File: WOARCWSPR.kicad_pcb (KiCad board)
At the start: 2 copper layers, 65 x 30.5 mm, 27 parts, among them J1 TP2, J2 Raspberry_Pi_2_3, J3 TP2, J4 Conn_Coaxial, J5 LPF_OUT, J6 LPF_IN, J7 TP1, J8 TP2, Q1 BS170, SW1 SW_Push_Dual

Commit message: Correct pin layout for filter board
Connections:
- C3 pad 2: Net-(J6-Pin_3) -> Net-(J6-Pin_1)
- J6 pad 1: GND -> Net-(J6-Pin_1)
- J6 pad 2: GND -> Net-(J6-Pin_1)
- J6 pad 3: Net-(J6-Pin_3) -> GND
- J6 pad 4: Net-(J6-Pin_3) -> GND
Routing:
- net Net-(J6-Pin_3): track 18.0 -> 0.00 mm
- net GND: track 82.5 -> 100.5 mm
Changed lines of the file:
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@@
 	(net 36 "Net-(Q1-G)")
 	(net 37 "Net-(J7-Pin_1)")
-	(net 38 "Net-(J6-Pin_3)")
+	(net 38 "Net-(J6-Pin_1)")
 	(net 39 "Net-(J8-Pin_1)")
 	(net 40 "Net-(R3-Pad1)")
@@
 			)
 		)
-		(property "Description" "Unpolarized capacitor"
+		(property "Description" "Polarized capacitor"
 			(at 0 0 0)
 			(unlocked yes)
@@
 			)
 		)
-		(property ki_fp_filters "C_*")
+		(property ki_fp_filters "CP_*")
 		(sheetname "Root")
 		(sheetfile "WOARCWSPR.kicad_sch")
@@
 			(layers "*.Cu" "*.Mask")
 			(remove_unused_layers no)
-			(net 38 "Net-(J6-Pin_3)")
+			(net 38 "Net-(J6-Pin_1)")
 			(pintype "passive")
 		)
@@
 			(layers "*.Cu" "*.Mask")
 			(remove_unused_layers no)
-			(net 1 "GND")
+			(net 38 "Net-(J6-Pin_1)")
 			(pinfunction "Pin_1")
 			(pintype "passive")
@@
 			(layers "*.Cu" "*.Mask")
 			(remove_unused_layers no)
-			(net 1 "GND")
+			(net 38 "Net-(J6-Pin_1)")
 			(pinfunction "Pin_2")
 			(pintype "passive")
@@
 			(layers "*.Cu" "*.Mask")
 			(remove_unused_layers no)
-			(net 38 "Net-(J6-Pin_3)")
+			(net 1 "GND")
 			(pinfunction "Pin_3")
 			(pintype "passive")
@@
 			(layers "*.Cu" "*.Mask")
 			(remove_unused_layers no)
-			(net 38 "Net-(J6-Pin_3)")
+			(net 1 "GND")
 			(pinfunction "Pin_4")
 			(pintype "passive")
@@
 	)
 	(segment
+		(start 221.9 56.8)
+		(end 220.8 57.9)
+		(width 0.2)
+		(layer "F.Cu")
+		(net 1)
+	)
+	(segment
 		(start 161.6 37.2)
 		(end 161.5 37.3)
@@
 	)
 	(segment
+		(start 220.8 57.9)
+		(end 214.5 57.9)
+		(width 0.2)
+		(layer "F.Cu")
+		(net 1)
+	)
+	(segment
+		(start 209.32 52.72)
+		(end 209 52.72)
+		(width 0.2)
+		(layer "F.Cu")
+		(net 1)
+	)
+	(segment
 		(start 178.035 34.775)
 		(end 178.035 34.365)
@@
 	)
 	(segment
+		(start 214.5 57.9)
+		(end 209.32 52.72)
+		(width 0.2)
+		(layer "F.Cu")
+		(net 1)
+	)
+	(segment
 		(start 204.585 31.085)
 		(end 207.365 31.085)
@@
 	)
 	(segment
+		(start 209 52.72)
+		(end 209 50.18)
+		(width 0.2)
+		(layer "F.Cu")
+		(net 1)
+	)
+	(segment
 		(start 178.035 34.365)
 		(end 178.8 33.6)
@@
 	)
 	(segment
-		(start 221.9 56.8)
-		(end 220.8 57.9)
-		(width 0.2)
-		(layer "F.Cu")
-		(net 38)
-	)
-	(segment
-		(start 220.8 57.9)
-		(end 214.5 57.9)
-		(width 0.2)
-		(layer "F.Cu")
-		(net 38)
-	)
-	(segment
-		(start 209.32 52.72)
-		(end 209 52.72)
-		(width 0.2)
-		(layer "F.Cu")
-		(net 38)
-	)
-	(segment
-		(start 214.5 57.9)
-		(end 209.32 52.72)
-		(width 0.2)
-		(layer "F.Cu")
-		(net 38)
-	)
-	(segment
-		(start 209 52.72)
-		(end 209 50.18)
-		(width 0.2)
-		(layer "F.Cu")
-		(net 38)
-	)
-	(segment
 		(start 220 53.8)
 		(end 220 53.4)
@@
 		(min_thickness 0.25)
 		(filled_areas_thickness no)
-		(fill yes
+		(fill
 			(thermal_gap 0.5)
 			(thermal_bridge_width 0.5)

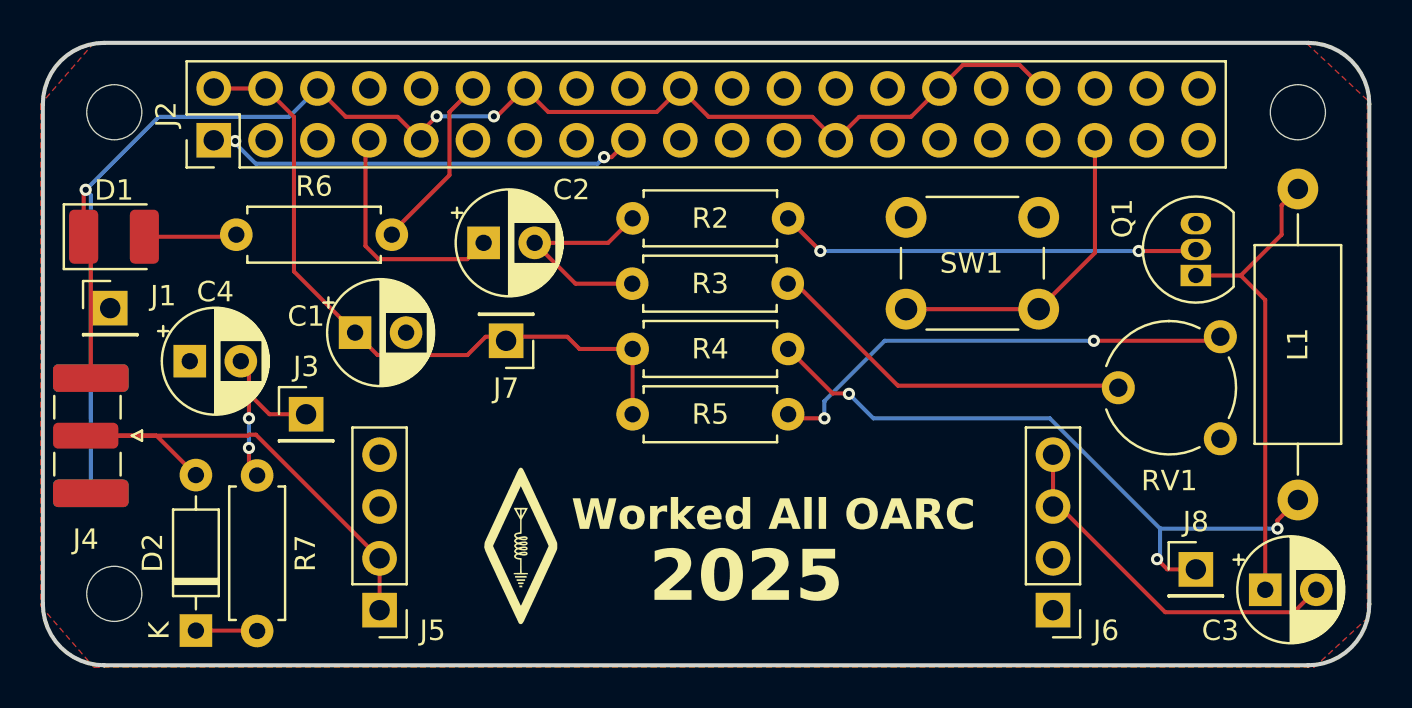
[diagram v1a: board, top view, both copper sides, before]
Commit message: Change to ceramic cap footprints
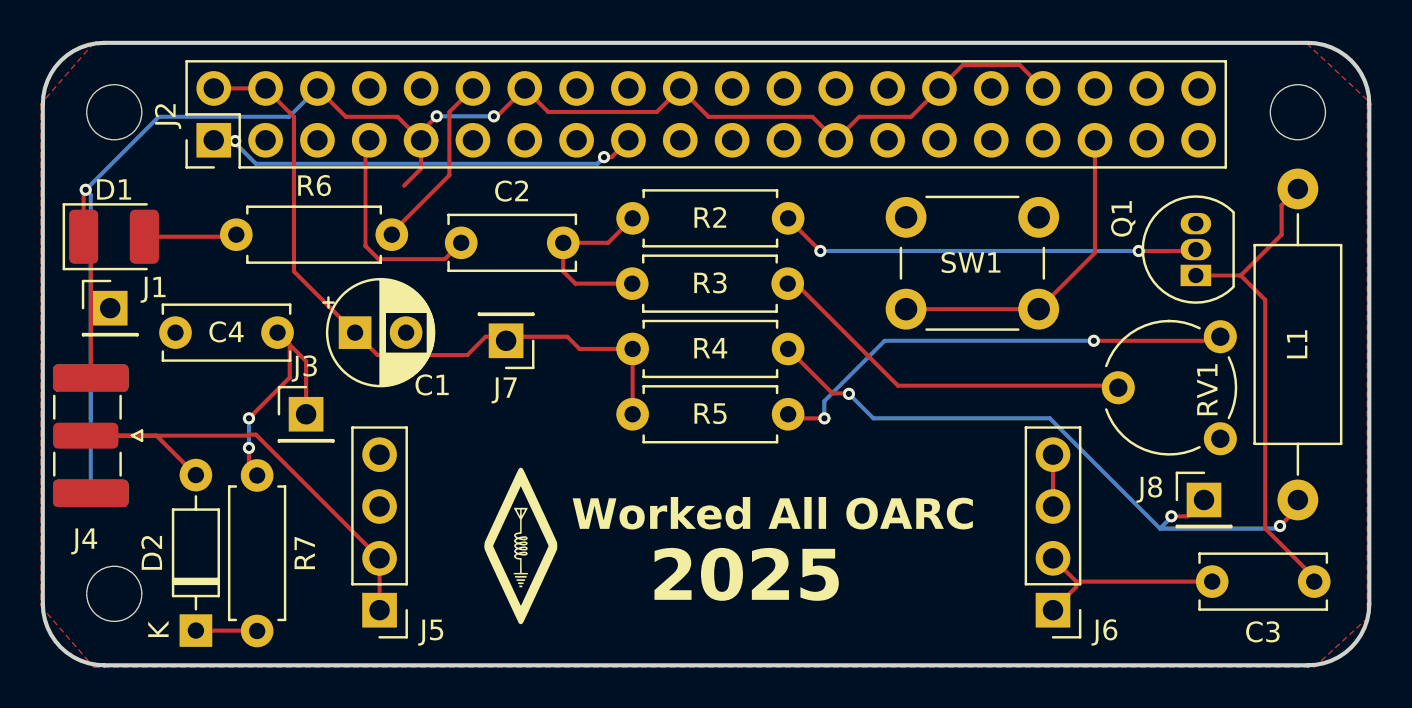
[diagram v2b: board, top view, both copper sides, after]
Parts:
- C2, C3, C4: footprint Capacitor_THT:CP_Radial_D5.0mm_P2.50mm -> Capacitor_THT:C_Disc_D6.0mm_W2.5mm_P5.00mm
- moved J8 3.42 mm to (216.4, 52.4)
- moved C3 2.43 mm to (221.8, 56.4), turned to 180 degrees
- moved C4 1.57 mm to (166.0, 44.2)
- moved C2 1.10 mm to (180.0, 39.8)
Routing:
- net GND: track 100.5 -> 87.9 mm
- net Net-(J6-Pin_1): track 0.00 -> 10.1 mm
- net Net-(J3-Pin_1): track 9.15 -> 12.8 mm
- net Net-(C2-Pad2): track 10.9 -> 8.93 mm
- net Net-(J2-GCLK0/GPIO4): track 11.7 -> 10.6 mm
- net Net-(J8-Pin_1): track 33.1 -> 32.2 mm
- net Net-(Q1-D): track 23.5 -> 24.1 mm

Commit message: Update version number to 1.1
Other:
- board text added: "WSPRHATZERO Version 1.1"
- board text removed: "WSPRHATZERO Version 1.0"
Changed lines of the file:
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@@
 		)
 	)
-	(gr_text "WSPRHATZERO\nVersion 1.0"
+	(gr_text "WSPRHATZERO\nVersion 1.1"
 		(at 207 55.6 0)
 		(layer "B.SilkS")
@@
 			(justify left bottom mirror)
 		)
-		(render_cache "WSPRHATZERO\nVersion 1.0" 0
+		(render_cache "WSPRHATZERO\nVersion 1.1" 0
 			(polygon
 				(pts
@@
 			(polygon
 				(pts
-					(xy 198.655605 54.182369) (xy 198.720692 54.199027) (xy 198.780439 54.226365) (xy 198.834093 54.264035)
-					(xy 198.880899 54.311689) (xy 198.894849 54.329733) (xy 198.92973 54.388186) (xy 198.952989 54.447009)
-					(xy 198.97109 54.515553) (xy 198.981933 54.577721) (xy 198.989605 54.646684) (xy 198.994166 54.722694)
-					(xy 198.995579 54.78448) (xy 198.995673 54.806006) (xy 198.994415 54.882598) (xy 198.990613 54.953276)
-					(xy 198.98422 55.018114) (xy 198.975193 55.077189) (xy 198.960137 55.143044) (xy 198.940808 55.200158)
-					(xy 198.911849 55.257367) (xy 198.875496 55.306972) (xy 198.832999 55.348743) (xy 198.784867 55.382444)
-					(xy 198.731609 55.407843) (xy 198.673736 55.424703) (xy 198.611758 55.43279) (xy 198.585931 55.433515)
-					(xy 198.526976 55.429733) (xy 198.461086 55.415316) (xy 198.400797 55.390295) (xy 198.346437 55.354857)
-					(xy 198.298328 55.309187) (xy 198.27672 55.282573) (xy 198.242383 55.224012) (xy 198.21923 55.16515)
-					(xy 198.201029 55.0969) (xy 198.190023 55.035386) (xy 198.18217 54.967601) (xy 198.177464 54.893427)
-					(xy 198.175994 54.833534) (xy 198.175896 54.812748) (xy 198.175956 54.807765) (xy 198.410956 54.807765)
-					(xy 198.411814 54.870403) (xy 198.414306 54.930715) (xy 198.419272 54.997468) (xy 198.427511 55.063641)
-					(xy 198.441437 55.122545) (xy 198.469425 55.174469) (xy 198.517621 55.216103) (xy 198.579661 55.232047)
-					(xy 198.585931 55.232161) (xy 198.644486 55.220899) (xy 198.695202 55.183719) (xy 198.723684 55.139545)
-					(xy 198.741025 55.080096) (xy 198.750942 55.012929) (xy 198.756771 54.942808) (xy 198.75964 54.876693)
-					(xy 198.760614 54.804541) (xy 198.759774 54.738998) (xy 198.757331 54.676283) (xy 198.752444 54.60729)
-					(xy 198.745609 54.548066) (xy 198.733807 54.489664) (xy 198.730425 54.479503) (xy 198.703026 54.426191)
-					(xy 198.659525 54.386118) (xy 198.598338 54.367134) (xy 198.585931 54.366662) (xy 198.527947 54.378408)
-					(xy 198.48041 54.412837) (xy 198.447885 54.462796) (xy 198.430544 54.523139) (xy 198.421843 54.581354)
-					(xy 198.415592 54.651944) (xy 198.412354 54.718975) (xy 198.410995 54.792401) (xy 198.410956 54.807765)
-					(xy 198.175956 54.807765) (xy 198.17661 54.753096) (xy 198.179798 54.679206) (xy 198.185574 54.611609)
-					(xy 198.193972 54.550135) (xy 198.208211 54.48164) (xy 198.226667 54.422108) (xy 198.254477 54.362027)
-					(xy 198.25972 54.35318) (xy 198.296074 54.303556) (xy 198.338579 54.261737) (xy 198.386733 54.22797)
-					(xy 198.440032 54.202504) (xy 198.497973 54.185588) (xy 198.560053 54.177468) (xy 198.585931 54.176739)
-				)
-			)
+					(xy 198.644549 54.574464) (xy 198.644549 55.396) (xy 198.40949 55.396) (xy 198.40949 54.204876)
+					(xy 198.565708 54.204876) (xy 198.589276 54.266019) (xy 198.625313 54.316963) (xy 198.673752 54.35764)
+					(xy 198.734527 54.387984) (xy 198.791984 54.404773) (xy 198.857257 54.414873) (xy 198.930314 54.418247)
+					(xy 198.930314 54.574464)
+				)
+			)

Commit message: Swap to 3mm THT LED
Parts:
- D1: footprint LED_SMD:LED_1210_3225Metric_Pad1.42x2.65mm_HandSolder -> LED_THT:LED_D3.0mm
- moved D1 1.55 mm to (161.6, 38.8)
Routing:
- net GND: track 87.9 -> 88.5 mm
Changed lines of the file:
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@@
 		)
 	)
-	(footprint "LED_SMD:LED_1210_3225Metric_Pad1.42x2.65mm_HandSolder"
+	(footprint "LED_THT:LED_D3.0mm"
 		(layer "F.Cu")
-		(at 162.9875 39.5)
-		(descr "LED SMD 1210 (3225 Metric), square (rectangular) end terminal, IPC_7351 nominal, (Body size source: http://www.tortai-tech.com/upload/download/2011102023233369053.pdf), generated with kicad-footprint-generator")
-		(tags "LED handsolder")
+		(at 161.6 38.8)
+		(descr "LED, diameter 3.0mm, 2 pins, generated by kicad-footprint-generator")
+		(tags "LED")
 		(property "Reference" "D1"
-			(at 0 -2.28 0)
+			(at 1.27 -2.96 0)
 			(layer "F.SilkS")
 			(effects
@@
 		)
 		(property "Value" "LED"
-			(at 0 2.28 0)
+			(at 1.27 2.96 0)
 			(layer "F.Fab")
 			(effects
@@
 			)
 		)
-		(property "Footprint" "LED_SMD:LED_1210_3225Metric_Pad1.42x2.65mm_HandSolder"
+		(property "Footprint" "LED_THT:LED_D3.0mm"
 			(at 0 0 0)
-			(unlocked yes)
 			(layer "F.Fab")
 			(hide yes)
@@
 		(property "Datasheet" ""
 			(at 0 0 0)
-			(unlocked yes)
 			(layer "F.Fab")
 			(hide yes)
@@
 		(property "Description" "Light emitting diode"
 			(at 0 0 0)
-			(unlocked yes)
 			(layer "F.Fab")
 			(hide yes)
@@
 		(sheetname "Root")
 		(sheetfile "WOARCWSPR.kicad_sch")
-		(attr smd)
+		(attr through_hole)
 		(fp_line
-			(start -2.46 -1.585)
-			(end -2.46 1.585)
+			(start -0.29 -1.236)
+			(end -0.29 -1.08)
 			(stroke
 				(width 0.12)
@@
 		)
 		(fp_line
-			(start -2.46 1.585)
-			(end 1.6 1.585)
+			(start -0.29 1.08)
+			(end -0.29 1.236)
 			(stroke
 				(width 0.12)
@@
 			(layer "F.SilkS")
 		)
-		(fp_line
-			(start 1.6 -1.585)
-			(end -2.46 -1.585)
+		(fp_arc
+			(start -0.29 -1.235516)
+			(mid 1.365624 -1.987701)
+			(end 2.941397 -1.080061)
 			(stroke
 				(width 0.12)
@@
 			(layer "F.SilkS")
 		)
-		(fp_line
-			(start -2.45 -1.58)
-			(end 2.45 -1.58)
+		(fp_arc
+			(start 0.229039 -1.08)
+			(mid 1.269965 -1.5)
+			(end 2.31091 -1.080049)
 			(stroke
-				(width 0.05)
+				(width 0.12)
 				(type solid)
 			)
-			(layer "F.CrtYd")
+			(layer "F.SilkS")
 		)
-		(fp_line
-			(start -2.45 1.58)
-			(end -2.45 -1.58)
+		(fp_arc
+			(start 2.31091 1.080049)
+			(mid 1.269965 1.5)
+			(end 0.229039 1.08)
 			(stroke
-				(width 0.05)
+				(width 0.12)
 				(type solid)
 			)
-			(layer "F.CrtYd")
+			(layer "F.SilkS")
+		)
+		(fp_arc
+			(start 2.941397 1.080061)
+			(mid 1.365624 1.987701)
+			(end -0.29 1.235516)
+			(stroke
+				(width 0.12)
+				(type solid)
+			)
+			(layer "F.SilkS")
 		)
 		(fp_line
-			(start 2.45 -1.58)
-			(end 2.45 1.58)
+			(start -1.15 -2.21)
+			(end -1.15 2.21)
 			(stroke
 				(width 0.05)
@@
 		)
 		(fp_line
-			(start 2.45 1.58)
-			(end -2.45 1.58)
+			(start -1.15 2.21)
+			(end 3.69 2.21)
 			(stroke
 				(width 0.05)
@@
 		)
 		(fp_line
-			(start -1.6 -0.625)
-			(end -1.6 1.25)
+			(start 3.69 -2.21)
+			(end -1.15 -2.21)
 			(stroke
-				(width 0.1)
+				(width 0.05)
 				(type solid)
 			)
-			(layer "F.Fab")
+			(layer "F.CrtYd")
 		)
 		(fp_line
-			(start -1.6 1.25)
-			(end 1.6 1.25)
+			(start 3.69 2.21)
+			(end 3.69 -2.21)
 			(stroke
-				(width 0.1)
+				(width 0.05)
 				(type solid)
 			)
-			(layer "F.Fab")
+			(layer "F.CrtYd")
 		)
 		(fp_line
-			(start -0.975 -1.25)
-			(end -1.6 -0.625)
+			(start -0.23 -1.16619)
+			(end -0.23 1.16619)
 			(stroke
 				(width 0.1)
@@
 			(layer "F.Fab")
 		)
-		(fp_line
-			(start 1.6 -1.25)
-			(end -0.975 -1.25)
+		(fp_arc
+			(start -0.23 -1.16619)
+			(mid 3.17 -0.000037)
+			(end -0.229955 1.166249)
 			(stroke
 				(width 0.1)
@@
 			(layer "F.Fab")
 		)
-		(fp_line
-			(start 1.6 1.25)
-			(end 1.6 -1.25)
+		(fp_circle
+			(center 1.27 0)
+			(end 2.77 0)
 			(stroke
 				(width 0.1)
 				(type solid)
 			)
+			(fill none)
 			(layer "F.Fab")
 		)
 		(fp_text user "${REFERENCE}"
-			(at 0.0125 0.1 0)
+			(at 1.27 0 0)
 			(layer "F.Fab")
 			(effects
@@
 			)
 		)
-		(pad "1" smd roundrect
-			(at -1.4875 0)
-			(size 1.425 2.65)
-			(layers "F.Cu" "F.Paste" "F.Mask")
-			(roundrect_rratio 0.175439)
+		(pad "1" thru_hole rect
+			(at 0 0)
+			(size 1.8 1.8)
+			(drill 0.9)
+			(layers "*.Cu" "*.Mask")
+			(remove_unused_layers no)
 			(net 1 "GND")
 			(pinfunction "K")
 			(pintype "passive")
 		)
-		(pad "2" smd roundrect
-			(at 1.4875 0)
-			(size 1.425 2.65)
-			(layers "F.Cu" "F.Paste" "F.Mask")
-			(roundrect_rratio 0.175439)
+		(pad "2" thru_hole circle
+			(at 2.54 0)
+			(size 1.8 1.8)
+			(drill 0.9)
+			(layers "*.Cu" "*.Mask")
+			(remove_unused_layers no)
 			(net 5 "Net-(D1-A)")
 			(pinfunction "A")
 			(pintype "passive")
 		)
-		(model "${KICAD8_3DMODEL_DIR}/LED_SMD.3dshapes/LED_1210_3225Metric.wrl"
+		(model "${KICAD8_3DMODEL_DIR}/LED_THT.3dshapes/LED_D3.0mm.wrl"
 			(offset
 				(xyz 0 0 0)
@@
 	)
 	(segment
-		(start 161.85 40.05)
-		(end 161.85 46.425)
+		(start 162.202082 36.602082)
+		(end 161.5 37.304164)
 		(width 0.2)
 		(layer "F.Cu")
@@
 	)
 	(segment
-		(start 161.6 37.2)
-		(end 161.5 37.3)
+		(start 203.435 32.235)
+		(end 204.585 31.085)
 		(width 0.2)
 		(layer "F.Cu")
@@
 	)
 	(segment
-		(start 203.435 32.235)
-		(end 204.585 31.085)
+		(start 178.035 34.775)
+		(end 176.885 33.625)
 		(width 0.2)
 		(layer "F.Cu")
@@
 	)
 	(segment
-		(start 178.035 34.775)
-		(end 176.885 33.625)
+		(start 161.5 39.7)
+		(end 161.85 40.05)
 		(width 0.2)
 		(layer "F.Cu")
@@
 	)
 	(segment
-		(start 161.5 37.3)
-		(end 161.5 39.5)
-		(width 0.2)
-		(layer "F.Cu")
-		(net 1)
-	)
-	(segment
 		(start 178.035 36.165)
 		(end 177.2 37)
@@
 	)
 	(segment
-		(start 203.435 32.235)
-		(end 202.045 33.625)
+		(start 161.5 37.304164)
+		(end 161.5 39.7)
 		(width 0.2)
 		(layer "F.Cu")
@@
 	)
 	(segment
-		(start 181.75 33.6)
-		(end 183.115 32.235)
+		(start 203.435 32.235)
+		(end 202.045 33.625)
 		(width 0.2)
 		(layer "F.Cu")
@@
 	)
 	(segment
-		(start 161.5 39.5)
-		(end 161.5 39.7)
+		(start 181.75 33.6)
+		(end 183.115 32.235)
 		(width 0.2)
 		(layer "F.Cu")
@@
 	)
 	(segment
-		(start 161.5 39.7)
-		(end 161.85 40.05)
+		(start 181.6 33.6)
+		(end 181.75 33.6)
 		(width 0.2)
 		(layer "F.Cu")
@@
 	)
 	(segment
-		(start 181.6 33.6)
-		(end 181.75 33.6)
+		(start 161.85 40.05)
+		(end 161.85 46.425)
 		(width 0.2)
 		(layer "F.Cu")
@@
 	)
 	(via
-		(at 161.6 37.2)
+		(at 162.202082 36.602082)
 		(size 0.6)
 		(drill 0.3)
@@
 	)
 	(segment
-		(start 172.955 32.235)
-		(end 171.565 33.625)
+		(start 161.85 36.954164)
+		(end 161.85 48.4)
 		(width 0.2)
 		(layer "B.Cu")
@@
 	)
 	(segment
-		(start 161.85 37.45)
-		(end 161.6 37.2)
+		(start 171.565 33.625)
+		(end 172.955 32.235)
 		(width 0.2)
 		(layer "B.Cu")
@@
 	)
 	(segment
-		(start 178.8 33.6)
-		(end 181.6 33.6)
+		(start 162.202082 36.602082)
+		(end 161.85 36.954164)
 		(width 0.2)
 		(layer "B.Cu")
@@
 	)
 	(segment
-		(start 161.85 48.4)
-		(end 161.85 37.45)
+		(start 178.8 33.6)
+		(end 181.6 33.6)
 		(width 0.2)
 		(layer "B.Cu")
@@
 	)
 	(segment
-		(start 161.85 48.4)
-		(end 161.85 52.075)
+		(start 165.179163 33.625)
+		(end 171.565 33.625)
 		(width 0.2)
 		(layer "B.Cu")
@@
 	)
 	(segment
-		(start 161.85 46.425)
-		(end 161.85 48.4)
+		(start 162.202082 36.602082)
+		(end 162.202082 36.602081)
 		(width 0.2)
 		(layer "B.Cu")
@@
 	)
 	(segment
-		(start 161.604163 37.2)
-		(end 161.6 37.2)
+		(start 161.85 48.4)
+		(end 161.85 52.075)
 		(width 0.2)
 		(layer "B.Cu")
@@
 	)
 	(segment
-		(start 165.179163 33.625)
-		(end 161.604163 37.2)
+		(start 161.85 46.425)
+		(end 161.85 48.4)
 		(width 0.2)
 		(layer "B.Cu")
@@
 	)
 	(segment
-		(start 171.565 33.625)
+		(start 162.202082 36.602081)
 		(end 165.179163 33.625)
 		(width 0.2)
